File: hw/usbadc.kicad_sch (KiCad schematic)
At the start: 14 parts, among them U6 PCA9306DC1, U8 24AA0x, X1 ECS-2520MV-260-CN-TR

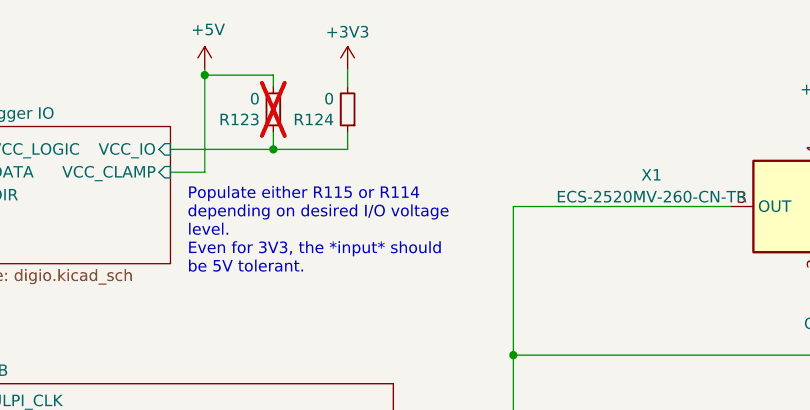
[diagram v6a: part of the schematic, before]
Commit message: [hw] added reset generator; removed 5V fill from FE area!
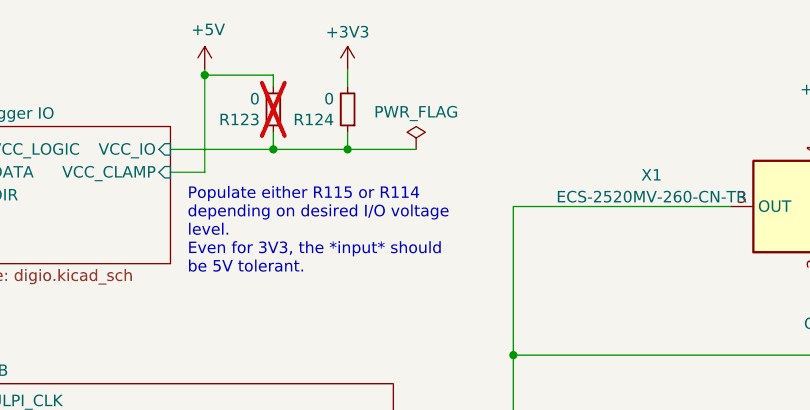
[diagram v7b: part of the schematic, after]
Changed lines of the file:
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@@
   (junction (at 83.185 164.465) (diameter 0) (color 0 0 0 0)
+  )
+  (junction (at 93.98 40.64) (diameter 0) (color 0 0 0 0)
   )
   (junction (at 78.105 32.385) (diameter 0) (color 0 0 0 0)
@@
   )
   (wire (pts (xy 232.41 156.21) (xy 235.585 156.21))
+    (stroke (width 0) (type default))
+  )
+  (wire (pts (xy 101.6 40.64) (xy 93.98 40.64))
     (stroke (width 0) (type default))
   )
@@
         )
       )
+    )
+  )
+  (symbol (lib_id "power:PWR_FLAG") (at 101.6 40.64 0) (unit 1)
+    (in_bom yes) (on_board yes) (dnp no) (fields_autoplaced)
+    (property "Reference" "#FLG07" (at 101.6 38.735 0)
+      (effects (font (size 1.27 1.27)) hide)
+    )
+    (property "Value" "PWR_FLAG" (at 101.6 36.5069 0)
+      (effects (font (size 1.27 1.27)))
+    )
+    (property "Footprint" "" (at 101.6 40.64 0)
+      (effects (font (size 1.27 1.27)) hide)
+    )
+    (property "Datasheet" "~" (at 101.6 40.64 0)
+      (effects (font (size 1.27 1.27)) hide)
+    )
+    (pin "1")
+    (instances
+      (project "usbadc"
+        (path "/7c8a1f8d-8834-4c9b-aaae-1f231e9b09a1"
+          (reference "#FLG07") (unit 1)
+        )
+      )

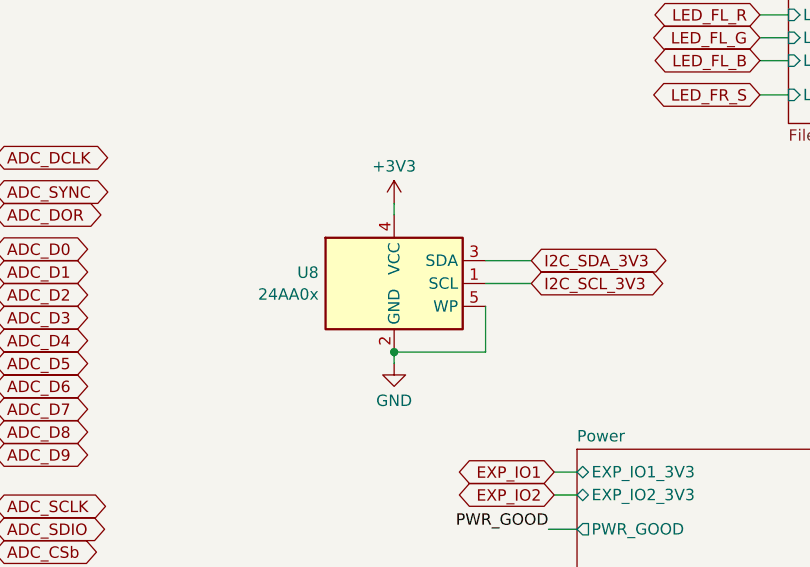
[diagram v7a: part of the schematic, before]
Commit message: [hw]: updated relay part no.
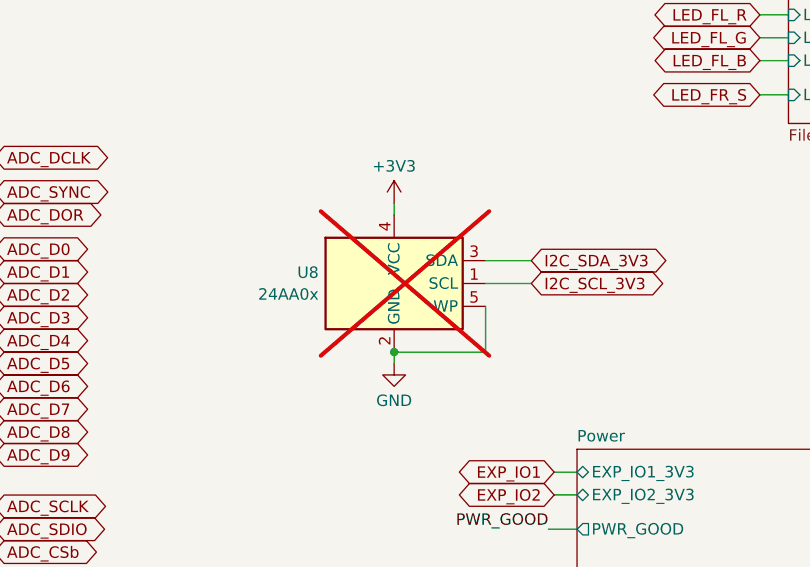
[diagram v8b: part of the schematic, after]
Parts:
- U8: now not fitted
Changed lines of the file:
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@@
   )
   (symbol (lib_id "fmc:24AA0x") (at 215.265 128.905 0) (unit 1)
-    (in_bom yes) (on_board yes) (dnp no) (fields_autoplaced)
+    (in_bom yes) (on_board yes) (dnp yes) (fields_autoplaced)
     (property "Reference" "U8" (at 206.883 127.6929 0)
       (effects (font (size 1.27 1.27)) (justify right))
